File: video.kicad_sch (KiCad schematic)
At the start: 55 parts, among them IC10 2318, IC11 MC14053, IC14 74LS86AN, IC21 74LS123N, IC22 74LS00N, IC23 74ALS74N, IC27 74LS20N, IC28 74LS393N, IC29 74LS393N, IC30 74LS32N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

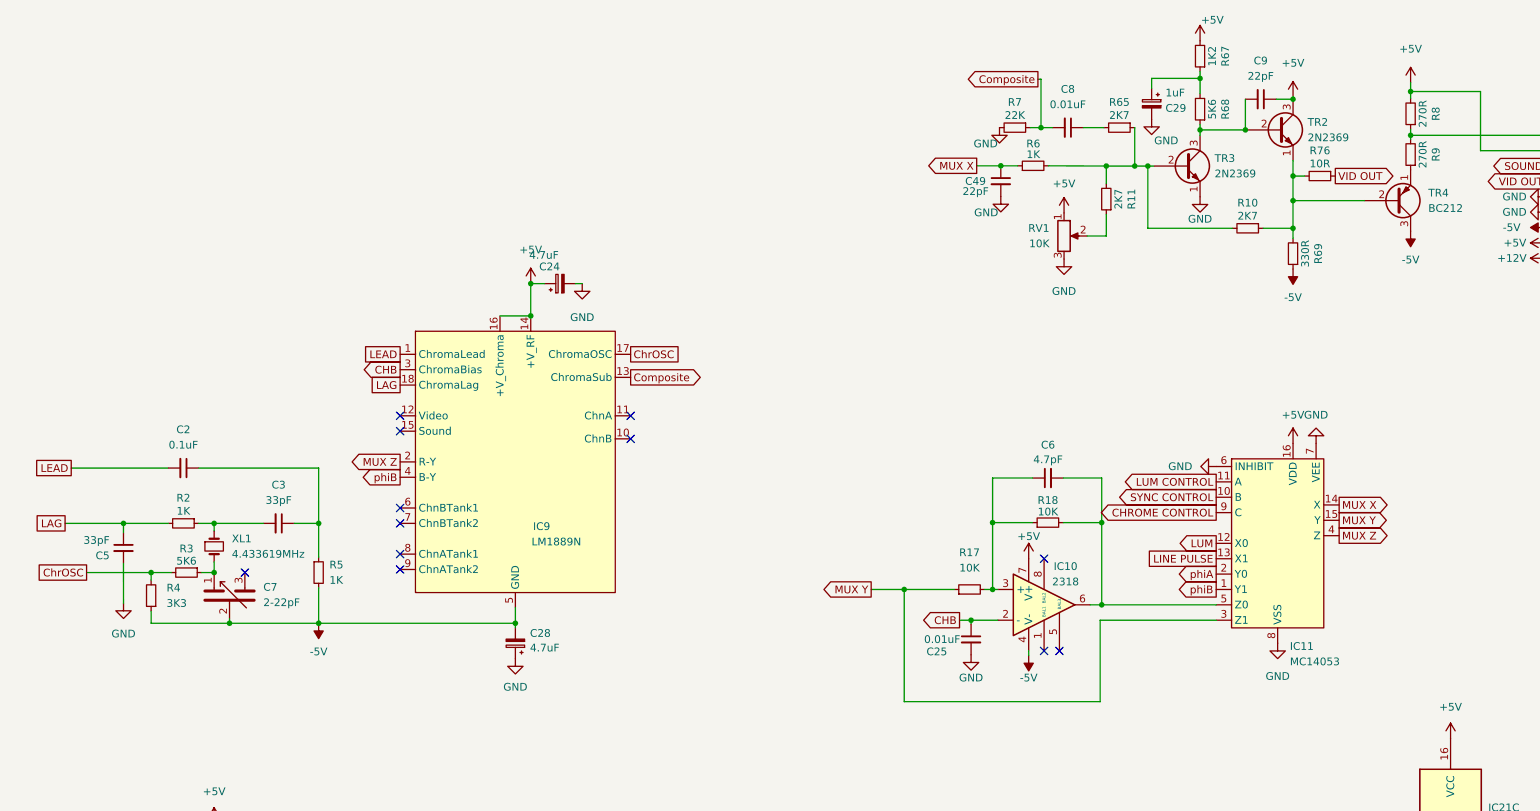
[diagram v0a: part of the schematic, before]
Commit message: fix inputs to video amp
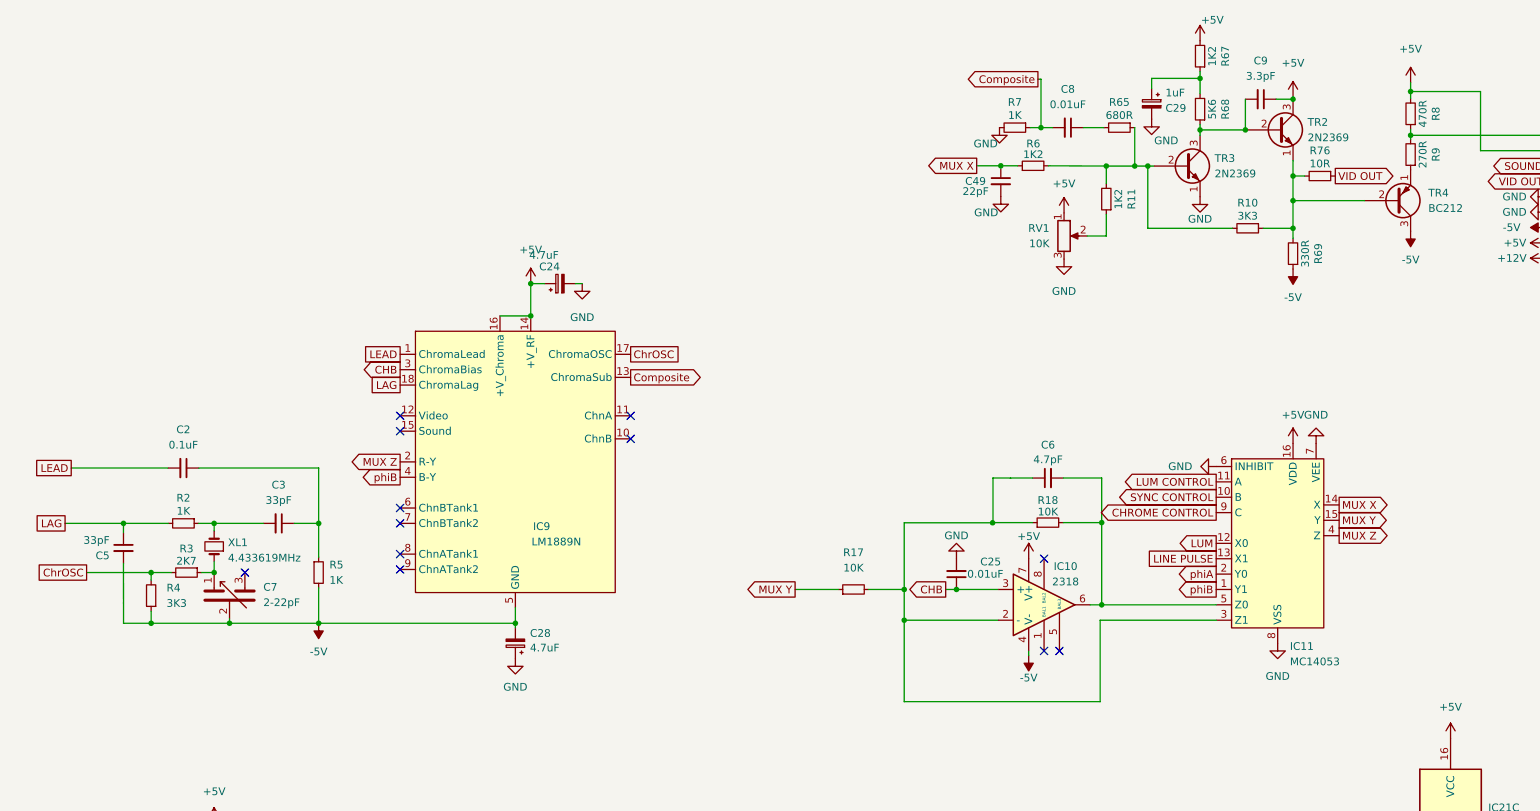
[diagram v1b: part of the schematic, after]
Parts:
- C9: value 22pF -> 3.3pF
- R10: value 2K7 -> 3K3
- R11: value 2K7 -> 1K2
- R3: value 5K6 -> 2K7
- R6: value 1K -> 1K2
- R65: value 2K7 -> 680R
- R7: value 22K -> 1K
- R8: value 270R -> 470R
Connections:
- net -5V: now also C5.2
- net CHB: now also IC10.3 (+); no longer IC10.2 (-)
- net GND: no longer C5.2
- net MUX Y: no longer IC11.3 (Z1)
- net at C3.2, R2.1: now also XL1.2; no longer XL1.1
- net at C6.1, R17.2, R18.1: now also IC10.2 (-), IC11.3 (Z1); no longer IC10.3 (+)
- net at C7.1, R3.1: now also XL1.1; no longer XL1.2
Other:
- moved on the sheet: C25, R17, XL1

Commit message: update notes
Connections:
- net Composite renamed Chrome
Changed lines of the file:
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@@
     )
   )
-  (global_label "Composite" (shape output) (at 295.148 28.448 180) (fields_autoplaced)
+  (global_label "Chrome" (shape output) (at 295.148 28.448 180) (fields_autoplaced)
     (effects (font (size 1.27 1.27)) (justify right))
-    (property "Intersheetrefs" "${INTERSHEET_REFS}" (at 282.9662 28.3686 0)
+    (property "Intersheetrefs" "${INTERSHEET_REFS}" (at 285.7603 28.448 0)
       (effects (font (size 1.27 1.27)) (justify right) hide)
     )
@@
     )
   )
-  (global_label "Composite" (shape output) (at 227.838 77.724 0) (fields_autoplaced)
+  (global_label "Chrome" (shape output) (at 227.838 77.724 0) (fields_autoplaced)
     (effects (font (size 1.27 1.27)) (justify left))
-    (property "Intersheetrefs" "${INTERSHEET_REFS}" (at 240.0198 77.6446 0)
+    (property "Intersheetrefs" "${INTERSHEET_REFS}" (at 237.2257 77.724 0)
       (effects (font (size 1.27 1.27)) (justify left) hide)
     )

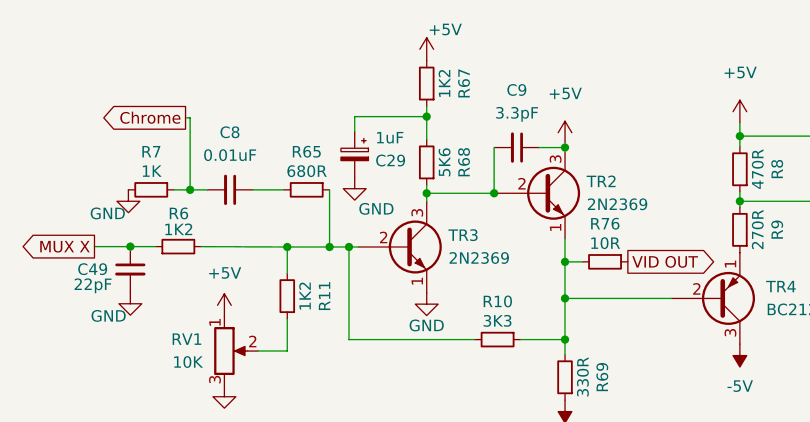
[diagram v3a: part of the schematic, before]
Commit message: fix video amp cap value
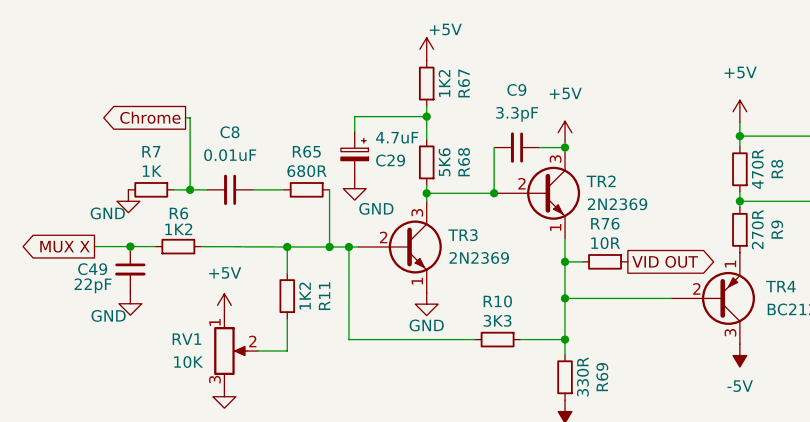
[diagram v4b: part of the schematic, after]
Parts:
- C29: value 1uF -> 4.7uF; DigiKey 732-8966-1-ND -> 478-8984-1-ND
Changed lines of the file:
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@@
       (effects (font (size 1.27 1.27)) (justify right))
     )
-    (property "Value" "1uF" (at 316.23 30.696 0)
+    (property "Value" "4.7uF" (at 316.23 30.696 0)
       (effects (font (size 1.27 1.27)) (justify right))
     )
@@
       (effects (font (size 1.27 1.27)) hide)
     )
-    (property "DigiKey" "732-8966-1-ND" (at 313.944 32.512 0)
+    (property "DigiKey" "478-8984-1-ND" (at 313.944 32.512 0)
       (effects (font (size 1.27 1.27)) hide)
     )

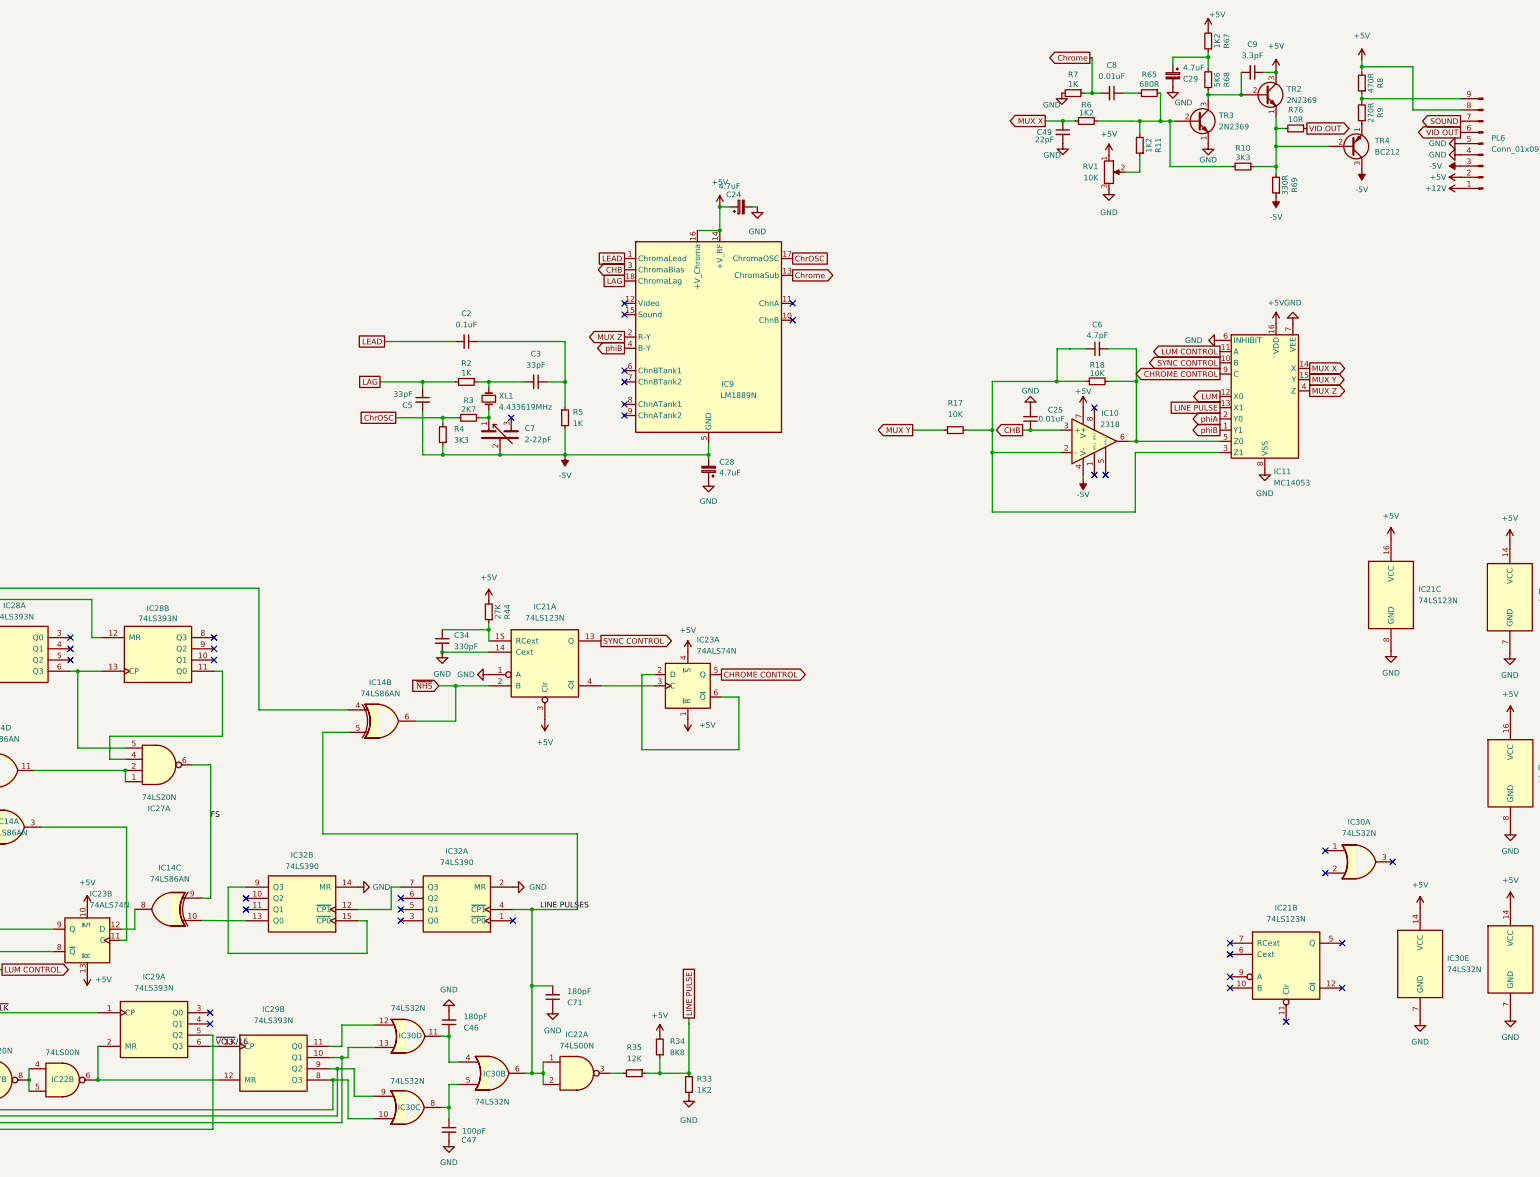
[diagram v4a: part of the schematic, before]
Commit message: revise video circuit
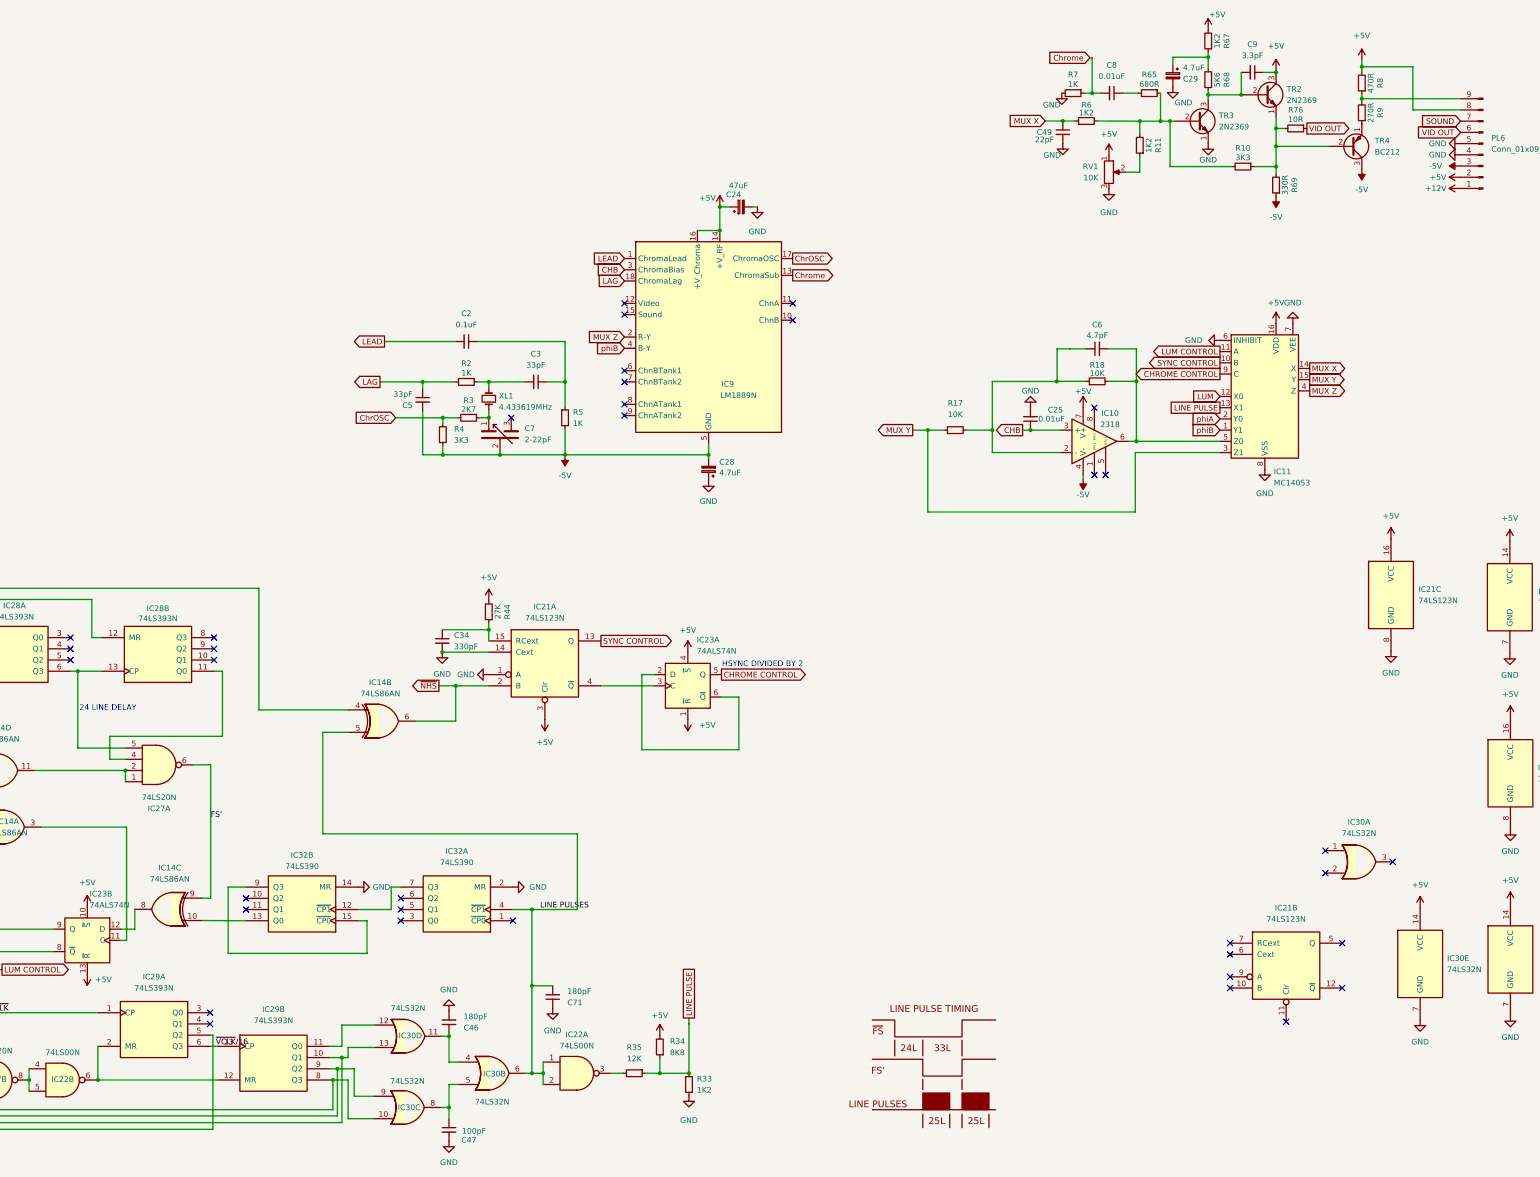
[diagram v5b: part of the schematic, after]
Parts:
- added U1: LINE_PULSE_DIAGRAM, symbol Dragon32_MKII:LINE_PULSE_DIAGRAM
- C24: value 4.7uF -> 47uF
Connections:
- net MUX Y: now also IC11.3 (Z1)
- net at C6.1, IC10.2 (-), R17.2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: no longer IC11.3 (Z1)
- net FS renamed FS'
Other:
- note added: "24 LINE DELAY"
- note added: "HSYNC DIVIDED BY 2"
